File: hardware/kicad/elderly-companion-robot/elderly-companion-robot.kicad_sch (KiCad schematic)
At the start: 0 parts

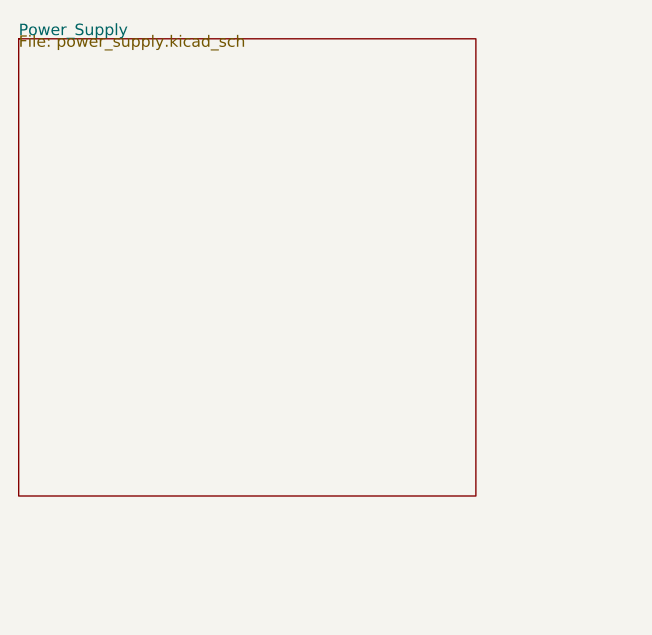
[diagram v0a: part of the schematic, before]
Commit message: Add net labels at ESP32 pin connection points and fix duplicate labels
- Placed net labels at all 28 ESP32-S3 signal pin connection points (x=38.10 left, x=63.50 right)
- Removed duplicate/overlapping labels from previous sessions that caused short circuits
- Fixed GPIO remapping: I2C_SCL→GPIO2, SERVO_PAN→GPIO42
- Labels connect by name to hierarchical labels for cross-sheet connectivity
- ERC shows 544 violations (mostly from unconnected wires and other sheets needing wiring)

Co-Authored-By: Claude Opus 4.7 <noreply@anthropic.com>
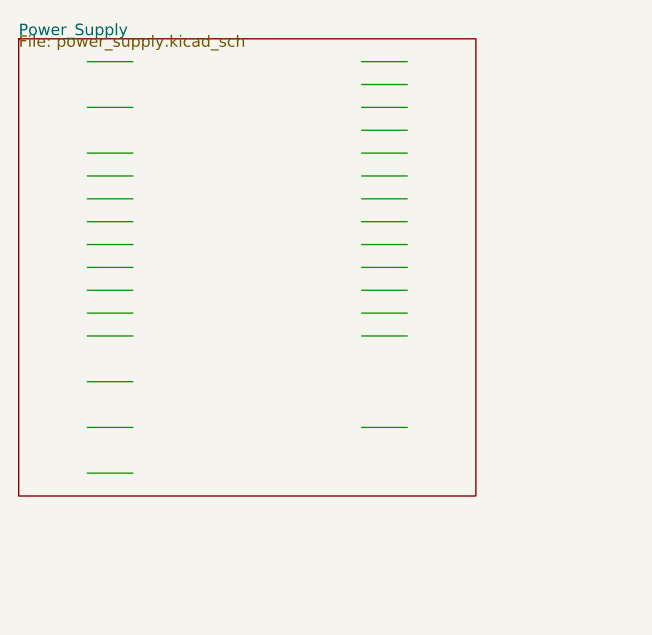
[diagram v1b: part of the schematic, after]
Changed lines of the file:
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@@
 		)
+	)
+	(wire
+		(pts (xy 33.02 27.94) (xy 38.1 27.94))
+		(stroke (width 0) (type solid))
+	)
+	(wire
+		(pts (xy 63.5 27.94) (xy 68.58 27.94))
+		(stroke (width 0) (type solid))
+	)
+	(wire
+		(pts (xy 63.5 30.48) (xy 68.58 30.48))
+		(stroke (width 0) (type solid))
+	)
+	(wire
+		(pts (xy 33.02 33.02) (xy 38.1 33.02))
+		(stroke (width 0) (type solid))
+	)
+	(wire
+		(pts (xy 63.5 33.02) (xy 68.58 33.02))
+		(stroke (width 0) (type solid))
+	)
+	(wire
+		(pts (xy 63.5 35.56) (xy 68.58 35.56))
+		(stroke (width 0) (type solid))
+	)
+	(wire
+		(pts (xy 33.02 38.1) (xy 38.1 38.1))
+		(stroke (width 0) (type solid))
+	)
+	(wire
+		(pts (xy 63.5 38.1) (xy 68.58 38.1))
+		(stroke (width 0) (type solid))
+	)
+	(wire
+		(pts (xy 33.02 40.64) (xy 38.1 40.64))
+		(stroke (width 0) (type solid))
+	)
+	(wire
+		(pts (xy 63.5 40.64) (xy 68.58 40.64))
+		(stroke (width 0) (type solid))
+	)
+	(wire
+		(pts (xy 33.02 43.18) (xy 38.1 43.18))
+		(stroke (width 0) (type solid))
+	)
+	(wire
+		(pts (xy 63.5 43.18) (xy 68.58 43.18))
+		(stroke (width 0) (type solid))
+	)
+	(wire
+		(pts (xy 33.02 45.72) (xy 38.1 45.72))
+		(stroke (width 0) (type solid))
+	)
+	(wire
+		(pts (xy 63.5 45.72) (xy 68.58 45.72))
+		(stroke (width 0) (type solid))
+	)
+	(wire
+		(pts (xy 33.02 48.26) (xy 38.1 48.26))
+		(stroke (width 0) (type solid))
+	)
+	(wire
+		(pts (xy 63.5 48.26) (xy 68.58 48.26))
+		(stroke (width 0) (type solid))
+	)
+	(wire
+		(pts (xy 33.02 50.8) (xy 38.1 50.8))
+		(stroke (width 0) (type solid))
+	)
+	(wire
+		(pts (xy 63.5 50.8) (xy 68.58 50.8))
+		(stroke (width 0) (type solid))
+	)
+	(wire
+		(pts (xy 33.02 53.34) (xy 38.1 53.34))
+		(stroke (width 0) (type solid))
+	)
+	(wire
+		(pts (xy 63.5 53.34) (xy 68.58 53.34))
+		(stroke (width 0) (type solid))
+	)
+	(wire
+		(pts (xy 33.02 55.88) (xy 38.1 55.88))
+		(stroke (width 0) (type solid))
+	)
+	(wire
+		(pts (xy 63.5 55.88) (xy 68.58 55.88))
+		(stroke (width 0) (type solid))
+	)
+	(wire
+		(pts (xy 33.02 58.42) (xy 38.1 58.42))
+		(stroke (width 0) (type solid))
+	)
+	(wire
+		(pts (xy 63.5 58.42) (xy 68.58 58.42))
+		(stroke (width 0) (type solid))
+	)
+	(wire
+		(pts (xy 33.02 63.5) (xy 38.1 63.5))
+		(stroke (width 0) (type solid))
+	)
+	(wire
+		(pts (xy 33.02 68.58) (xy 38.1 68.58))
+		(stroke (width 0) (type solid))
+	)
+	(wire
+		(pts (xy 63.5 68.58) (xy 68.58 68.58))
+		(stroke (width 0) (type solid))
+	)
+	(wire
+		(pts (xy 33.02 73.66) (xy 38.1 73.66))
+		(stroke (width 0) (type solid))
 	)
 	(sheet_instances
